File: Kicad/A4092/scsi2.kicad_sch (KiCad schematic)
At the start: 27 parts, among them U9 LSI53C770 SCSI Host Controller

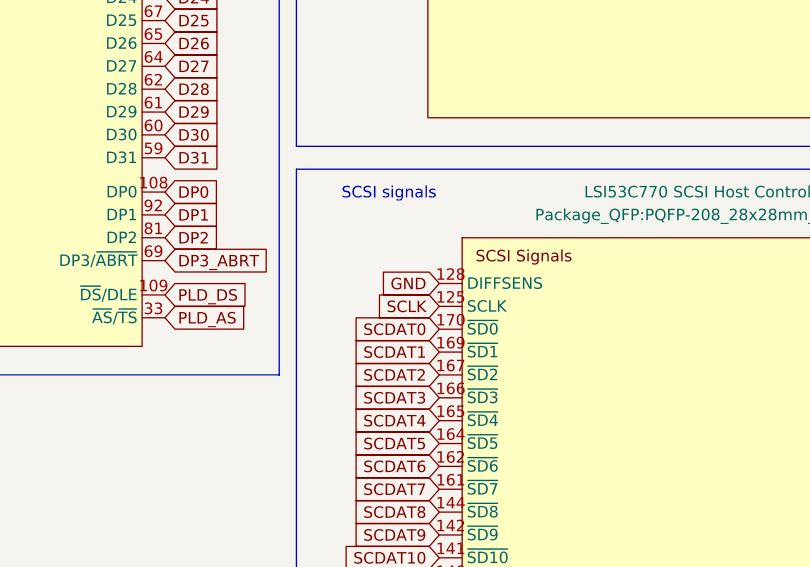
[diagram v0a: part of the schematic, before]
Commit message: Revert false change, DIFFSENS -> V5
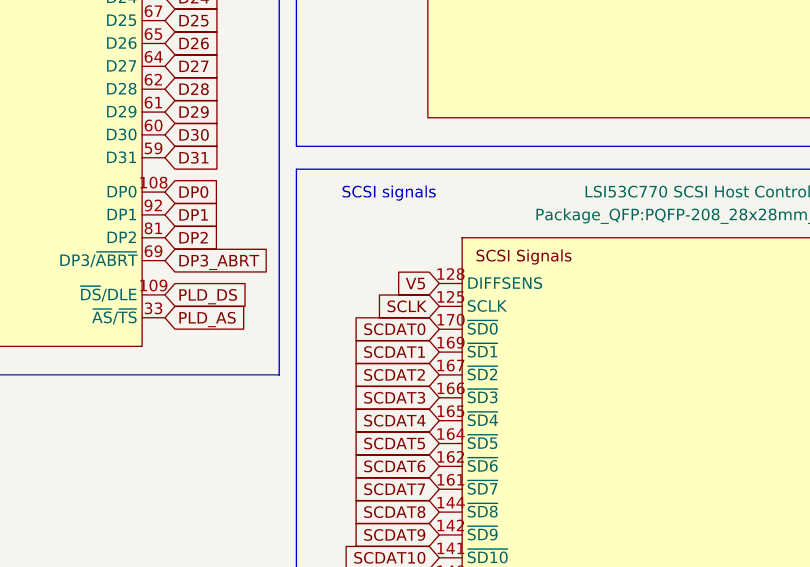
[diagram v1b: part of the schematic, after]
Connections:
- net GND: no longer U9.128 (DIFFSENS)
- net V5: now also U9.128 (DIFFSENS)
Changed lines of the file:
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@@
 		)
 	)
-	(global_label "GND"
+	(global_label "V5"
 		(shape input)
 		(at 109.22 116.84 180)
@@
 		)
 		(property "Intersheetrefs" "${INTERSHEET_REFS}"
-			(at 102.3643 116.84 0)
+			(at 103.9367 116.84 0)
 			(effects
 				(font

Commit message: Tie DIFFSENS to GND not V5
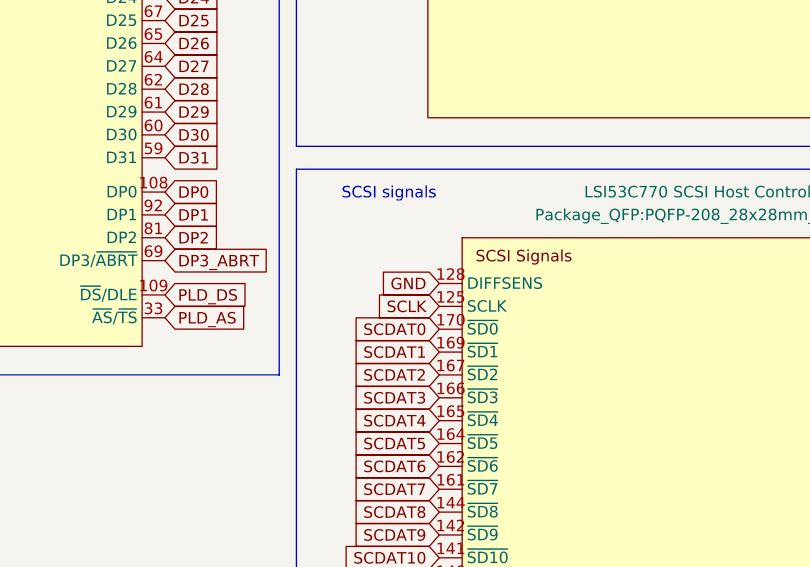
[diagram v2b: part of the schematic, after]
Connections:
- net GND: now also U9.128 (DIFFSENS)
- net V5: no longer U9.128 (DIFFSENS)
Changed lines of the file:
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@@
 		)
 	)
-	(global_label "V5"
+	(global_label "GND"
 		(shape input)
 		(at 109.22 116.84 180)
@@
 		)
 		(property "Intersheetrefs" "${INTERSHEET_REFS}"
-			(at 103.9367 116.84 0)
+			(at 102.3643 116.84 0)
 			(effects
 				(font
